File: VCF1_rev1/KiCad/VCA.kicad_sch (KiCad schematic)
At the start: 16 parts, among them U10 74HC4053, U11 LM13700, U8 Opamp_Quad

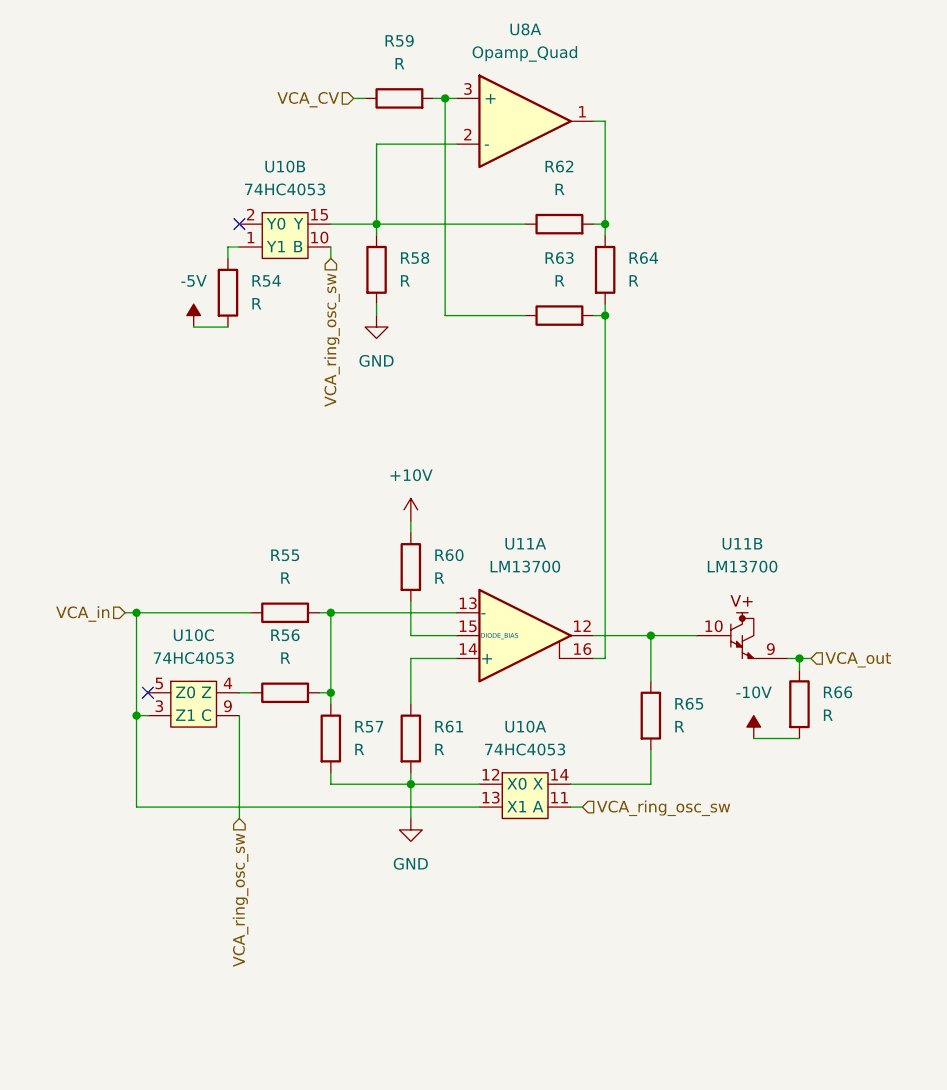
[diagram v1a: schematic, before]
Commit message: The filter blocks are more or less done, page order has gotten more sane for easier reading.
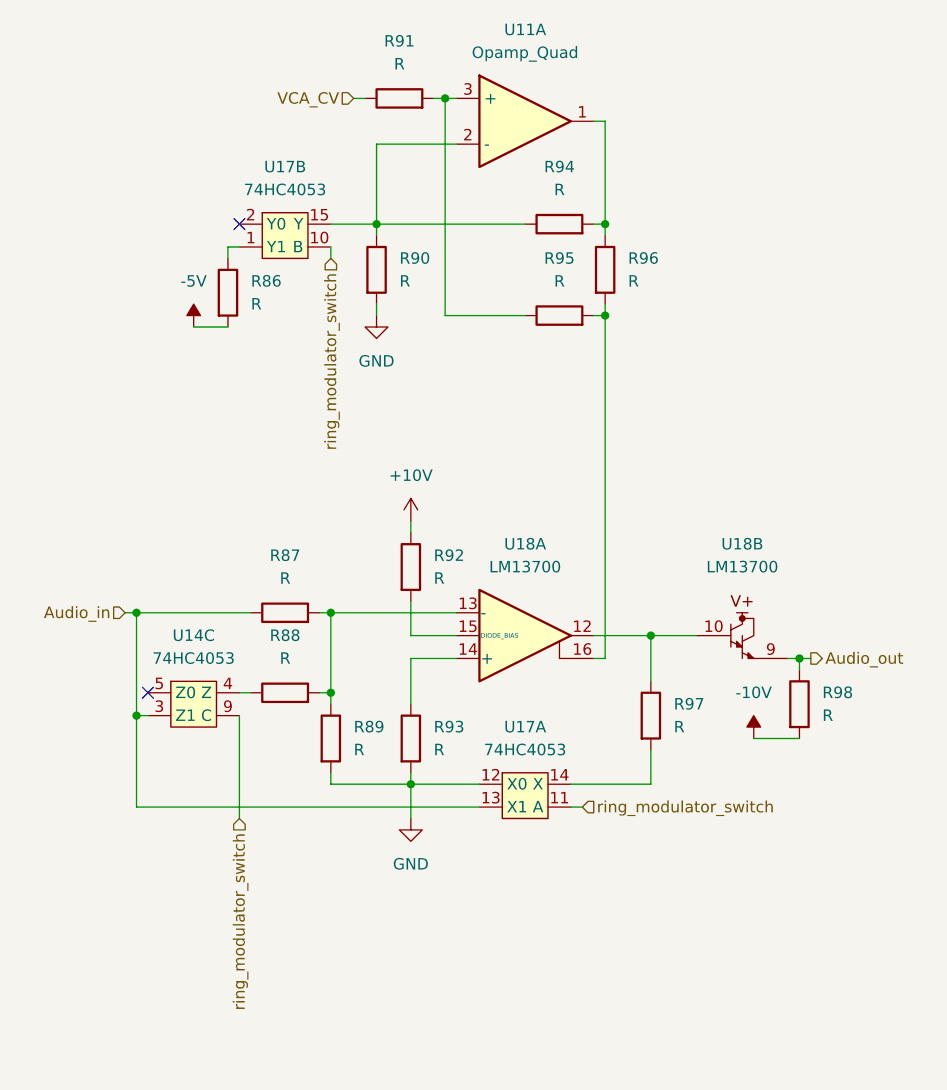
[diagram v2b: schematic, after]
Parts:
- renumbered R54 to R86, R55 to R87, R56 to R88, R57 to R89, R58 to R90, R59 to R91, R60 to R92, R61 to R93, R62 to R94, R63 to R95, R64 to R96, R65 to R97, R66 to R98, U8 to U11, U10 to U14, U10 to U17, U11 to U18
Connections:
- net VCA_in renamed Audio_in
- net VCA_out renamed Audio_out
- net VCA_ring_osc_sw renamed ring_modulator_switch

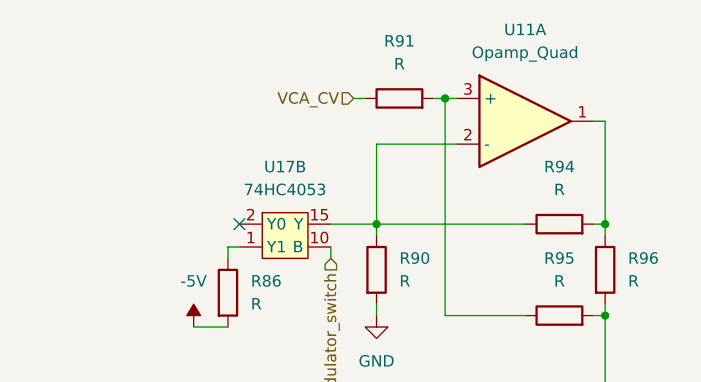
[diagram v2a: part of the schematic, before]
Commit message: Added the MUX. The signal path is now more or less complete!
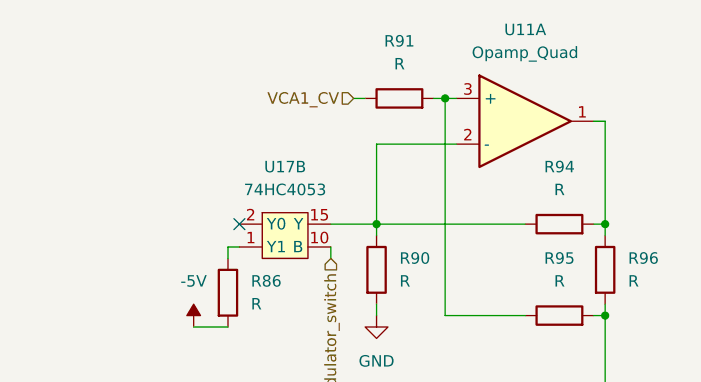
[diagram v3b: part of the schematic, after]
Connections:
- net VCA_CV renamed VCA1_CV
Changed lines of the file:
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@@
   (paper "A4")
   (junction (at 129.54 69.85) (diameter 0) (color 0 0 0 0))
-  (junction (at 77.47 114.3) (diameter 0) (color 0 0 0 0))
+  (junction (at 107.95 121.92) (diameter 0) (color 0 0 0 0))
+  (junction (at 151.13 107.95) (diameter 0) (color 0 0 0 0))
   (junction (at 129.54 59.69) (diameter 0) (color 0 0 0 0))
   (junction (at 111.76 45.72) (diameter 0) (color 0 0 0 0))
   (junction (at 134.62 105.41) (diameter 0) (color 0 0 0 0))
+  (junction (at 99.06 102.87) (diameter 0) (color 0 0 0 0))
   (junction (at 104.14 59.69) (diameter 0) (color 0 0 0 0))
-  (junction (at 107.95 121.92) (diameter 0) (color 0 0 0 0))
-  (junction (at 99.06 102.87) (diameter 0) (color 0 0 0 0))
+  (junction (at 77.47 114.3) (diameter 0) (color 0 0 0 0))
+  (junction (at 99.06 111.76) (diameter 0) (color 0 0 0 0))
   (junction (at 77.47 102.87) (diameter 0) (color 0 0 0 0))
-  (junction (at 151.13 107.95) (diameter 0) (color 0 0 0 0))
-  (junction (at 99.06 111.76) (diameter 0) (color 0 0 0 0))
   (no_connect (at 88.9 59.69))
   (no_connect (at 78.74 111.76))
-  (wire (pts (xy 104.14 50.8) (xy 113.03 50.8))
+  (wire (pts (xy 104.14 50.8) (xy 104.14 59.69))
     (stroke (width 0) (type default) (color 0 0 0 0))
   )
-  (wire (pts (xy 104.14 50.8) (xy 104.14 59.69))
+  (wire (pts (xy 104.14 50.8) (xy 113.03 50.8))
     (stroke (width 0) (type default) (color 0 0 0 0))
   )
@@
     (stroke (width 0) (type default) (color 0 0 0 0))
   )
+  (wire (pts (xy 129.54 69.85) (xy 129.54 68.58))
+    (stroke (width 0) (type default) (color 0 0 0 0))
+  )
   (wire (pts (xy 128.27 107.95) (xy 129.54 107.95))
     (stroke (width 0) (type default) (color 0 0 0 0))
   )
-  (wire (pts (xy 129.54 69.85) (xy 129.54 68.58))
+  (wire (pts (xy 107.95 113.03) (xy 107.95 107.95))
     (stroke (width 0) (type default) (color 0 0 0 0))
   )
   (wire (pts (xy 107.95 107.95) (xy 113.03 107.95))
-    (stroke (width 0) (type default) (color 0 0 0 0))
-  )
-  (wire (pts (xy 107.95 113.03) (xy 107.95 107.95))
     (stroke (width 0) (type default) (color 0 0 0 0))
   )
@@
     (stroke (width 0) (type default) (color 0 0 0 0))
   )
+  (wire (pts (xy 120.65 69.85) (xy 111.76 69.85))
+    (stroke (width 0) (type default) (color 0 0 0 0))
+  )
   (wire (pts (xy 111.76 69.85) (xy 111.76 45.72))
     (stroke (width 0) (type default) (color 0 0 0 0))
   )
   (wire (pts (xy 111.76 45.72) (xy 113.03 45.72))
-    (stroke (width 0) (type default) (color 0 0 0 0))
-  )
-  (wire (pts (xy 120.65 69.85) (xy 111.76 69.85))
     (stroke (width 0) (type default) (color 0 0 0 0))
   )
@@
     (stroke (width 0) (type default) (color 0 0 0 0))
   )
-  (wire (pts (xy 129.54 48.26) (xy 129.54 59.69))
+  (wire (pts (xy 128.27 48.26) (xy 129.54 48.26))
     (stroke (width 0) (type default) (color 0 0 0 0))
   )
-  (wire (pts (xy 128.27 48.26) (xy 129.54 48.26))
+  (wire (pts (xy 129.54 48.26) (xy 129.54 59.69))
     (stroke (width 0) (type default) (color 0 0 0 0))
   )
@@
     (stroke (width 0) (type default) (color 0 0 0 0))
   )
-  (wire (pts (xy 134.62 105.41) (xy 139.7 105.41))
+  (wire (pts (xy 128.27 105.41) (xy 134.62 105.41))
     (stroke (width 0) (type default) (color 0 0 0 0))
   )
-  (wire (pts (xy 128.27 105.41) (xy 134.62 105.41))
+  (wire (pts (xy 134.62 105.41) (xy 139.7 105.41))
     (stroke (width 0) (type default) (color 0 0 0 0))
   )
@@
     (effects (font (size 1.27 1.27)) (justify right))
   )
-  (hierarchical_label "VCA_CV" (shape input) (at 101.6 45.72 180)
+  (hierarchical_label "VCA1_CV" (shape input) (at 101.6 45.72 180)
     (effects (font (size 1.27 1.27)) (justify right))
   )

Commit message: Lot of work on panel etc.
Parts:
- renumbered R90 to R100, R91 to R101, R92 to R102, R93 to R103, R94 to R104, R95 to R105, R96 to R106, R97 to R107, R98 to R108, R86 to R96, R87 to R97, R88 to R98, R89 to R99, U11 to U14, U14 to U15, U17 to U18, U18 to U19

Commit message: Cleaned up the first page with the overview and tried to make it a bit more readable.
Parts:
- renumbered R96 to R106, R97 to R107, R98 to R108, R99 to R109, R100 to R110, R101 to R111, R102 to R112, R103 to R113, R104 to R114, R105 to R115, R106 to R116, R107 to R117, R108 to R118
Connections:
- net ring_modulator_switch renamed Ring_modulator_select

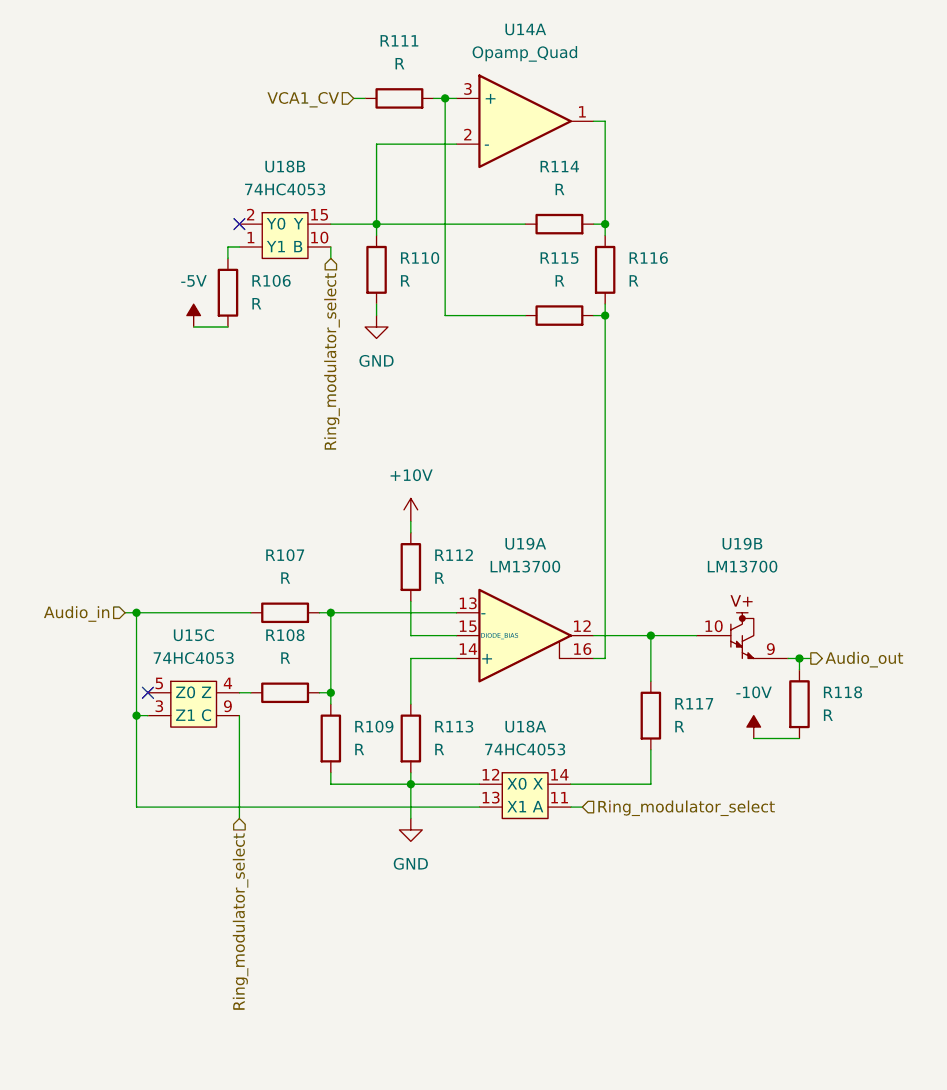
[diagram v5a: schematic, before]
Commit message: Drew a better symbol for LM13700 because the other one was ugly.
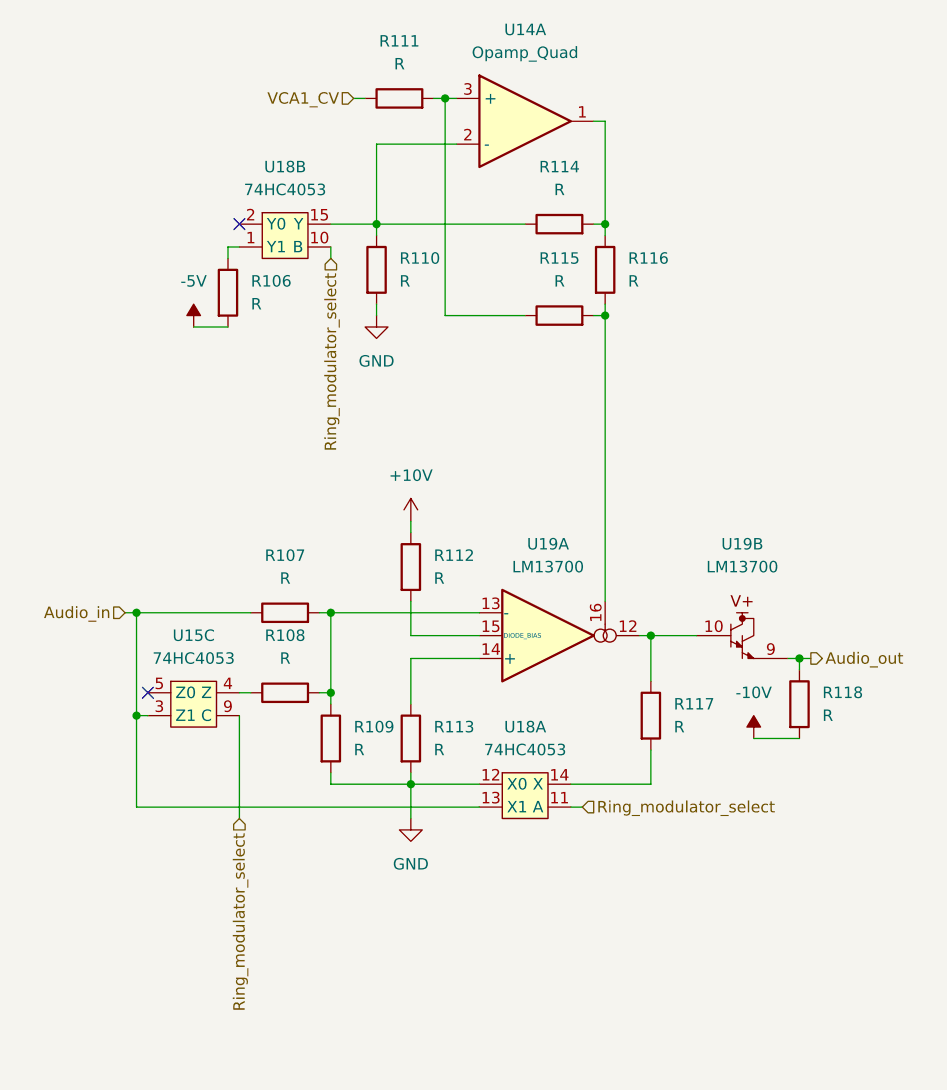
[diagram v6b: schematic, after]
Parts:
- removed U19: LM13700, symbol Amplifier_Operational:LM13700
- added U19: LM13700, symbol Modular_Mayhem:LM13700
- R106, R107, R108, R109, R110, R111, R112, R113, R114, R115, R116, R117, R118: footprint (none) -> Resistor_SMD:R_0603_1608Metric
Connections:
- net Audio_out: now also U19.9
- net at R112.2: now also U19.15 (DIODE_BIAS)
- net at R117.1: now also U19.10, U19.12
- net at R107.2, R108.2, R109.1: now also U19.13 (-)
- net at R113.1: now also U19.14 (+)
- net at R115.2, R116.2: now also U19.16

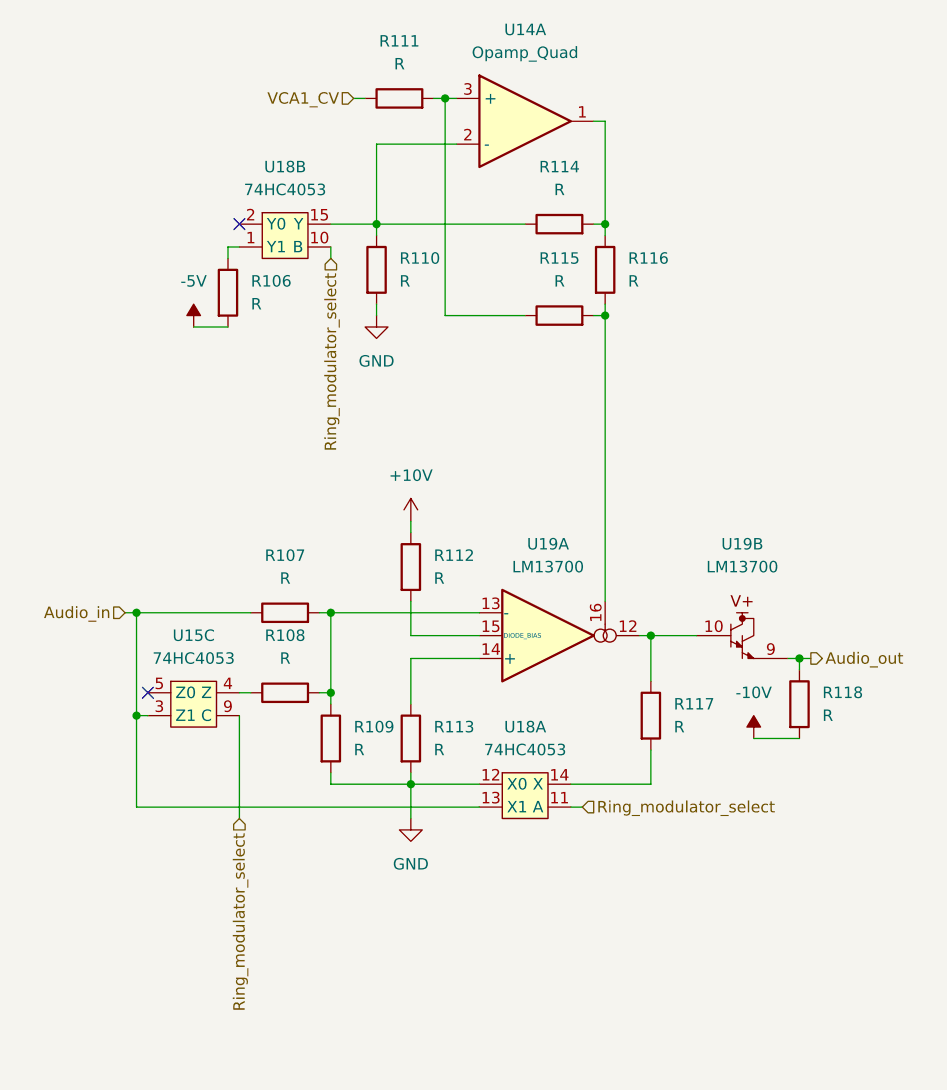
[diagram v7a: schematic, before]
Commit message: Started to populate the PCB and done some small fixes in the schematics.
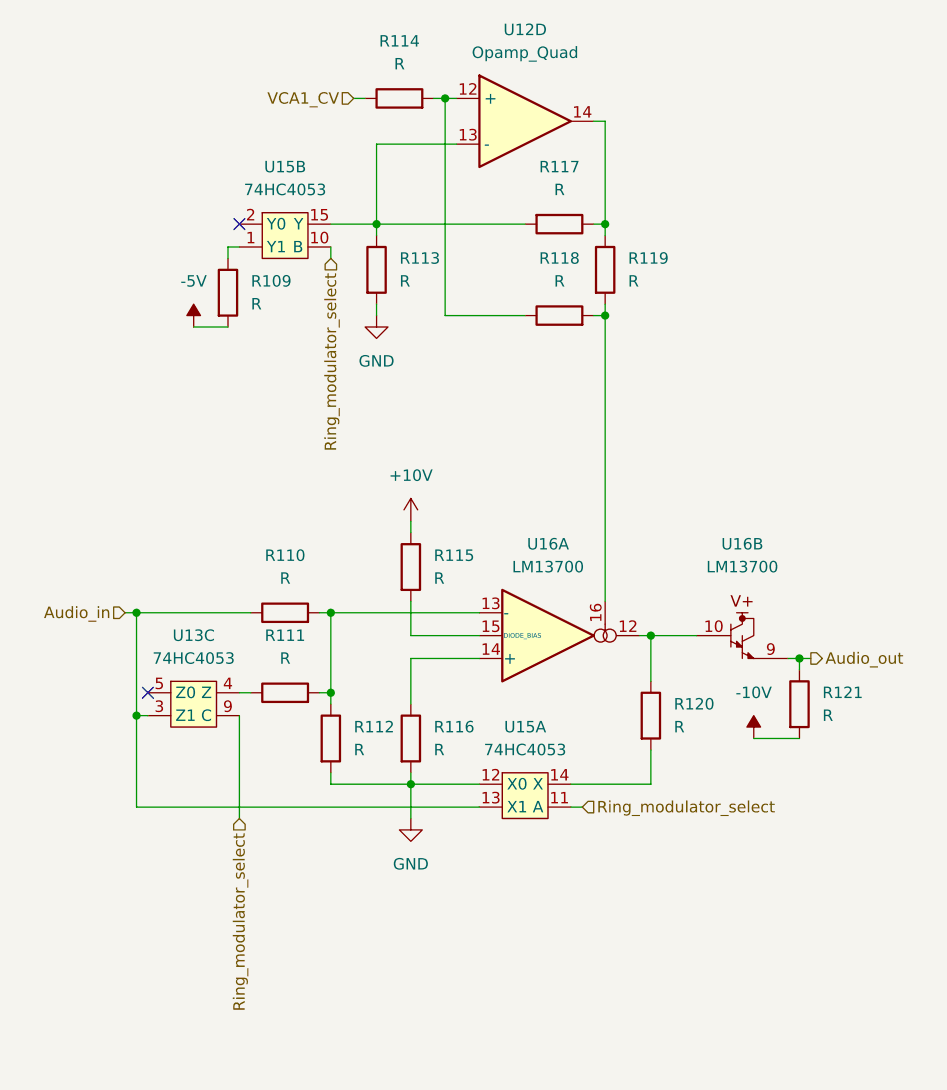
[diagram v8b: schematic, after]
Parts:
- U12: renamed from U14; footprint (none) -> Package_SO:SOIC-14_3.9x8.7mm_P1.27mm
- U13: renamed from U15; footprint (none) -> Package_SO:SOIC-16_3.9x9.9mm_P1.27mm
- U15: renamed from U18; footprint (none) -> Package_SO:SOIC-16_3.9x9.9mm_P1.27mm
- U16: renamed from U19; footprint (none) -> Package_SO:SOIC-16_3.9x9.9mm_P1.27mm
- renumbered R106 to R109, R107 to R110, R108 to R111, R109 to R112, R110 to R113, R111 to R114, R112 to R115, R113 to R116, R114 to R117, R115 to R118, R116 to R119, R117 to R120, R118 to R121
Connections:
- net at R113.1, U15.15 (Y): now also R117.2, U12.13 (-); no longer R117.1, U12.2 (-)
- net at R114.2, R118.1: now also U12.12 (+); no longer U12.3 (+)
- new net: R117.1, R119.1, U12.14
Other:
- moved on the sheet: R117
